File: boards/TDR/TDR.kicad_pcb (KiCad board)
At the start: 4 copper layers, 60 x 37 mm, 138 parts, among them J1 USB_C_Receptacle_USB2.0, J2 SMA, U1 LFE5UM5G-45-CABGA381, U10 W25Q128JVPIQ, U11 93LCxxBxxOT, U12 FT2232HL, U13 MIC5504-3.3YM5, U14 Resistive_Power_Divider, U15 MCP4822, U2 USBLC6-2SC6, U3 AxxDBF1-200.0000, U4 TLV3541, U5 MIC5504-3.3YM5, U6 AP3402, U7 AP3402, U8 LD39050PUR, U9 LD39050PUR, Y1 12MHz

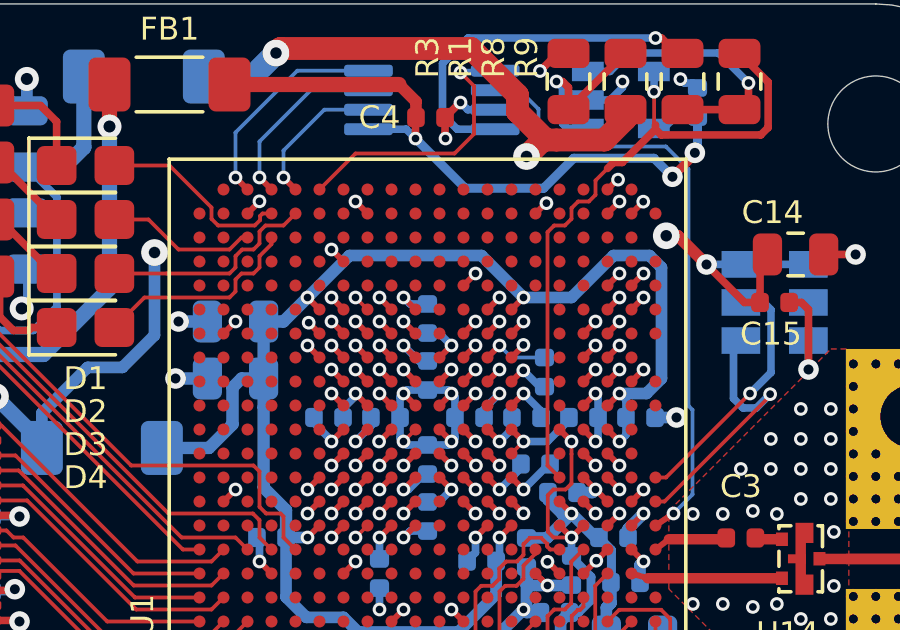
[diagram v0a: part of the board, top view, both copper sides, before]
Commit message: finishing touches on the silkscreen
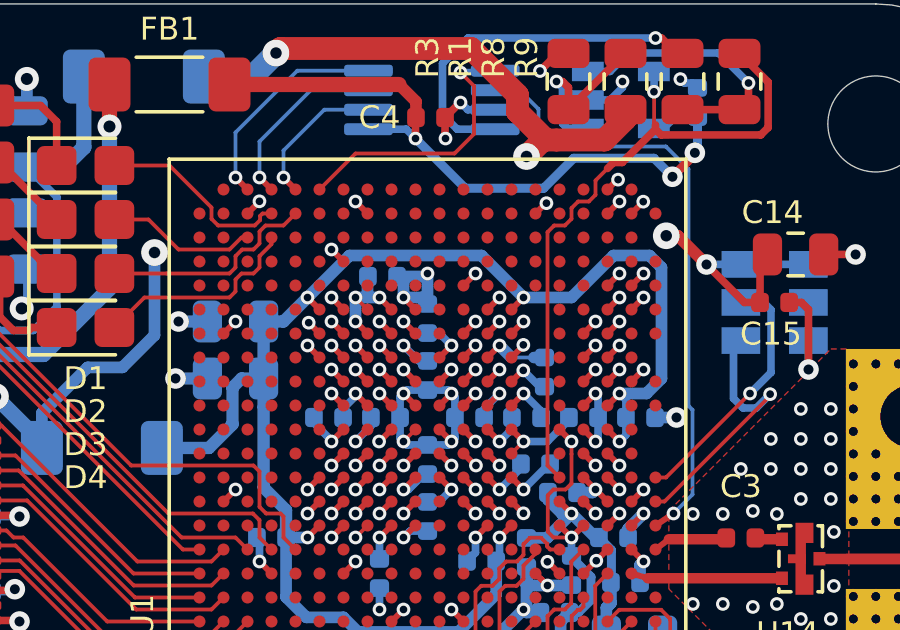
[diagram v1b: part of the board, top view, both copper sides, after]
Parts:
- added C25: 100n, Capacitor_SMD:C_0402_1005Metric, B.Cu at (146.6, 72.1)
- moved REF** 22.2 mm to (119.3, 91.0)
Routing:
- net GND: track 203.9 -> 206.8 mm, vias 183 -> 184
- net +3V3: track 54.2 -> 55.8 mm

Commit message: hopefully PCB is done
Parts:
- added C27: 1u, Capacitor_SMD:C_0805_2012Metric, B.Cu at (137.9, 85.8)
- added C29: 1u, Capacitor_SMD:C_0805_2012Metric, B.Cu at (137.9, 80.0)
- added C31: 100n, Capacitor_SMD:C_0402_1005Metric, F.Cu at (151.2, 65.9)
- added TP1: TestPoint, TestPoint:TestPoint_Pad_D1.0mm, F.Cu at (158.7, 86.6)
- added U16: MIC5504-3.3YM5, Package_TO_SOT_SMD:SOT-23-5, B.Cu at (137.9, 82.9)
- moved FB1 2.04 mm to (141.5, 66.1), turned to 180 degrees
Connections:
- C4 pad 1: Net-(C23-Pad1) -> Net-(C29-Pad1)
- C58 pad 2: Net-(C58-Pad2) -> /FT2232H/3.3V_FTDI
- FB1 pad 1: /5V_INPUT -> Net-(C29-Pad1)
- R32 pad 1: Net-(C58-Pad2) -> /FT2232H/3.3V_FTDI
- R34 pad 1: Net-(C58-Pad2) -> /FT2232H/3.3V_FTDI
- R35 pad 1: Net-(C58-Pad2) -> /FT2232H/3.3V_FTDI
- U1 pad T8: /OUT_A -> /OUT_B
- U1 pad Y6: /OUT_B -> /OUT_A
- U11 pad 6: Net-(C58-Pad2) -> /FT2232H/3.3V_FTDI
- U15 pad 1: Net-(C23-Pad1) -> Net-(C29-Pad1)
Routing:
- net Net-(C29-Pad1): track 0.00 -> 30.2 mm, vias 0 -> 2
- net /FT2232H/3.3V_FTDI: track 88.6 -> 106.3 mm, vias 5 -> 6
- net /5V_INPUT: track 118.0 -> 128.2 mm, vias 7 -> 6
- net Net-(C58-Pad2): track 7.62 -> 0.00 mm
- net Net-(TP1-Pad1): track 0.00 -> 5.28 mm
- net /OUT_B: track 20.5 -> 16.0 mm
- net GND: track 206.8 -> 211.1 mm, vias 184 -> 187
- net /OUT_A: track 22.7 -> 25.8 mm, vias 1 -> 2
- net Net-(C31-Pad2): track 6.29 -> 7.87 mm
- net Net-(C23-Pad1): track 23.3 -> 24.8 mm
- net /FT2232H/1.8V: track 37.1 -> 38.2 mm
- net +2V5: track 121.7 -> 121.0 mm
- net /VCCA: track 47.7 -> 48.2 mm
- net /~CS: track 9.34 -> 9.47 mm, vias 1 -> 3

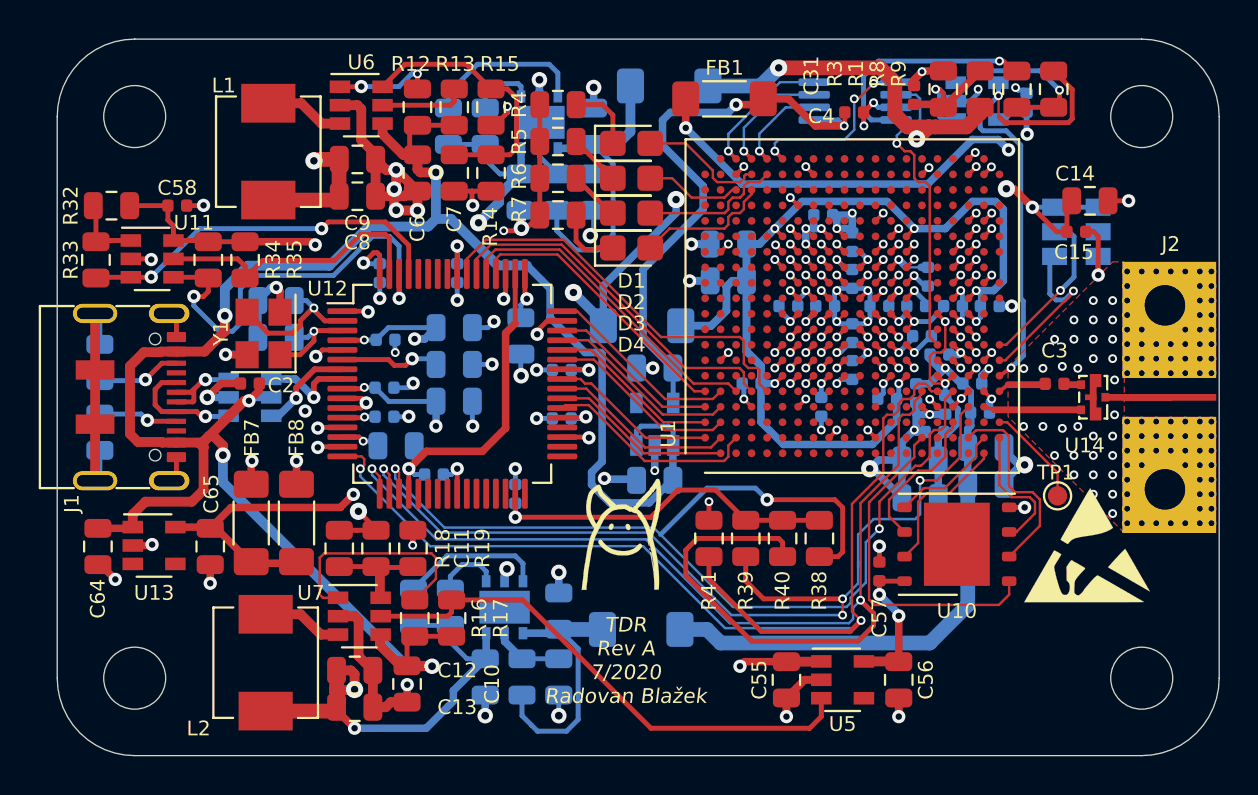
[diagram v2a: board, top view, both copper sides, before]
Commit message: Add LD39050PUR feedback resistor values, fixed regulator enable
Fixes #1
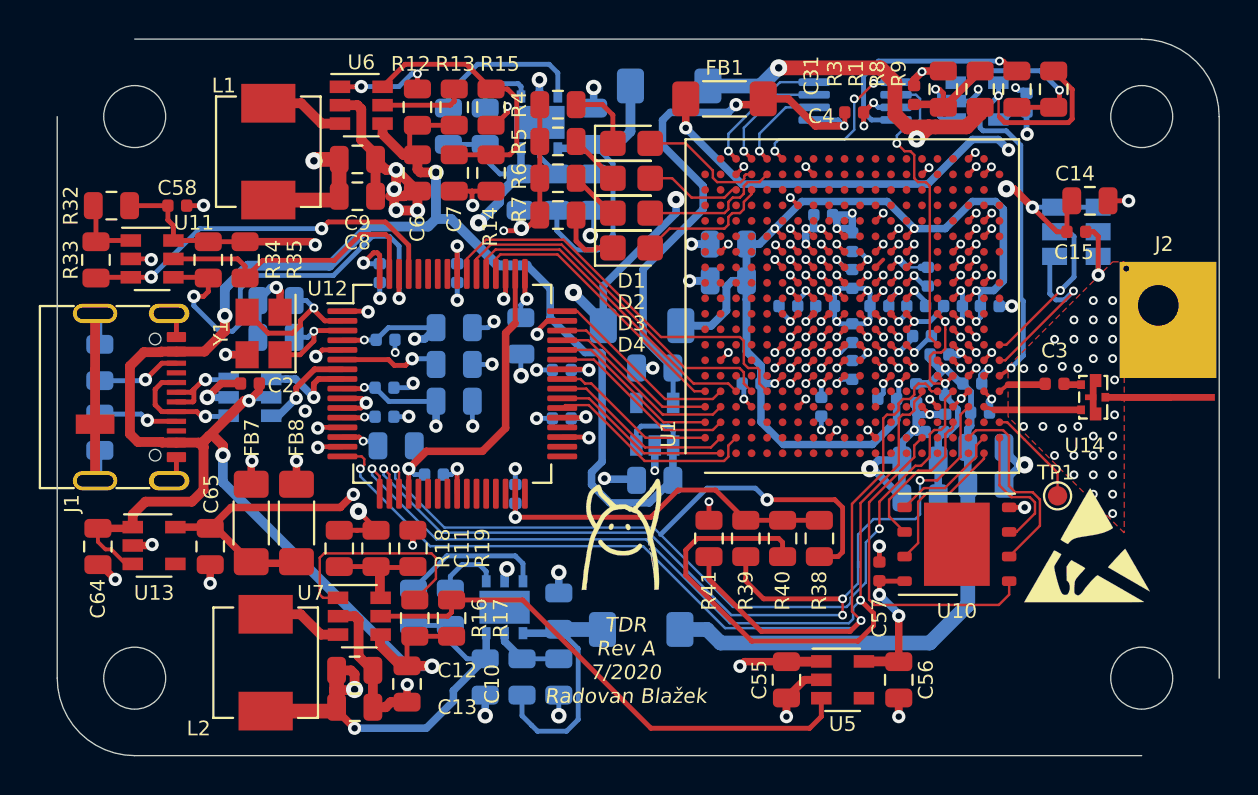
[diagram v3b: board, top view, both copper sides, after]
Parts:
- R1, R3, R8, R9: value 470 -> 4.7k
- R24, R26: value TBD -> 24k
- R25, R27: value TBD -> 47k
- U3: value AxxDBF1-200.0000 -> AK5DBF1-200.0000
- U4: value TLV3541 -> MCP6V81T-E/OT
- moved J2 0.34 mm to (164.2, 81.5)
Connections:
- net /FPGA_PROGRAMN renamed Net-(U1-PadW3)
- U1 pad A10: Net-(U1-PadA10) -> (no net)
- U1 pad A11: Net-(U1-PadA11) -> (no net)
- U1 pad A12: Net-(U1-PadA12) -> (no net)
- U1 pad A13: Net-(U1-PadA13) -> (no net)
- U1 pad A14: Net-(U1-PadA14) -> (no net)
- U1 pad A15: Net-(U1-PadA15) -> (no net)
- U1 pad A16: Net-(U1-PadA16) -> (no net)
- U1 pad A17: Net-(U1-PadA17) -> (no net)
- U1 pad A18: Net-(U1-PadA18) -> (no net)
- U1 pad A19: Net-(U1-PadA19) -> (no net)
- U1 pad A6: Net-(U1-PadA6) -> (no net)
- U1 pad A7: Net-(U1-PadA7) -> (no net)
- U1 pad A8: Net-(U1-PadA8) -> (no net)
- U1 pad A9: Net-(U1-PadA9) -> (no net)
- U1 pad B10: Net-(U1-PadB10) -> (no net)
- U1 pad B11: Net-(U1-PadB11) -> (no net)
- U1 pad B12: Net-(U1-PadB12) -> (no net)
- U1 pad B13: Net-(U1-PadB13) -> (no net)
- U1 pad B15: Net-(U1-PadB15) -> (no net)
- U1 pad B16: Net-(U1-PadB16) -> (no net)
- U1 pad B17: Net-(U1-PadB17) -> (no net)
- U1 pad B18: Net-(U1-PadB18) -> (no net)
- U1 pad B19: Net-(U1-PadB19) -> (no net)
- U1 pad B20: Net-(U1-PadB20) -> (no net)
- U1 pad B6: Net-(U1-PadB6) -> (no net)
- U1 pad B8: Net-(U1-PadB8) -> (no net)
- U1 pad B9: Net-(U1-PadB9) -> (no net)
- U1 pad C10: Net-(U1-PadC10) -> (no net)
- U1 pad C11: Net-(U1-PadC11) -> (no net)
- U1 pad C12: Net-(U1-PadC12) -> (no net)
- U1 pad C13: Net-(U1-PadC13) -> (no net)
- U1 pad C14: Net-(U1-PadC14) -> (no net)
- U1 pad C15: Net-(U1-PadC15) -> (no net)
- U1 pad C16: Net-(U1-PadC16) -> (no net)
- U1 pad C17: Net-(U1-PadC17) -> (no net)
- U1 pad C6: Net-(U1-PadC6) -> (no net)
- U1 pad C7: Net-(U1-PadC7) -> (no net)
- U1 pad C8: Net-(U1-PadC8) -> (no net)
- U1 pad C9: Net-(U1-PadC9) -> (no net)
- U1 pad D10: Net-(U1-PadD10) -> (no net)
- U1 pad D11: Net-(U1-PadD11) -> (no net)
- U1 pad D12: Net-(U1-PadD12) -> (no net)
- U1 pad D13: Net-(U1-PadD13) -> (no net)
- U1 pad D14: Net-(U1-PadD14) -> (no net)
- U1 pad D15: Net-(U1-PadD15) -> (no net)
- U1 pad D16: Net-(U1-PadD16) -> (no net)
- U1 pad D6: Net-(U1-PadD6) -> (no net)
- U1 pad D7: Net-(U1-PadD7) -> (no net)
- U1 pad D8: Net-(U1-PadD8) -> (no net)
- U1 pad D9: Net-(U1-PadD9) -> (no net)
- U1 pad E10: Net-(U1-PadE10) -> (no net)
- U1 pad E11: Net-(U1-PadE11) -> (no net)
- U1 pad E12: Net-(U1-PadE12) -> (no net)
- U1 pad E13: Net-(U1-PadE13) -> (no net)
- U1 pad E14: Net-(U1-PadE14) -> (no net)
- U1 pad E15: Net-(U1-PadE15) -> (no net)
- U1 pad E6: Net-(U1-PadE6) -> (no net)
- U1 pad E7: Net-(U1-PadE7) -> (no net)
- U1 pad E8: Net-(U1-PadE8) -> (no net)
- U1 pad E9: Net-(U1-PadE9) -> (no net)
- U1 pad F1: Net-(U1-PadF1) -> (no net)
- U1 pad F10: Net-(U1-PadF10) -> (no net)
- U1 pad F11: Net-(U1-PadF11) -> (no net)
- U1 pad F12: Net-(U1-PadF12) -> (no net)
- U1 pad F9: Net-(U1-PadF9) -> (no net)
- U1 pad G1: Net-(U1-PadG1) -> (no net)
- U1 pad G2: Net-(U1-PadG2) -> (no net)
- U1 pad H1: Net-(U1-PadH1) -> (no net)
- U1 pad H2: Net-(U1-PadH2) -> (no net)
- U1 pad J1: Net-(U1-PadJ1) -> (no net)
- U1 pad J3: Net-(U1-PadJ3) -> (no net)
- U1 pad J4: Net-(U1-PadJ4) -> (no net)
- U1 pad J5: Net-(U1-PadJ5) -> (no net)
- U1 pad K1: Net-(U1-PadK1) -> (no net)
- U1 pad K2: Net-(U1-PadK2) -> (no net)
- U1 pad K3: Net-(U1-PadK3) -> (no net)
- U1 pad K4: Net-(U1-PadK4) -> (no net)
- U1 pad K5: Net-(U1-PadK5) -> (no net)
- U1 pad L1: Net-(U1-PadL1) -> (no net)
- U1 pad L14: Net-(U1-PadL14) -> (no net)
- U1 pad L15: Net-(U1-PadL15) -> (no net)
- U1 pad L16: Net-(U1-PadL16) -> (no net)
- U1 pad L17: Net-(U1-PadL17) -> (no net)
- U1 pad L18: Net-(U1-PadL18) -> (no net)
- U1 pad L19: Net-(U1-PadL19) -> (no net)
- U1 pad L2: Net-(U1-PadL2) -> (no net)
- U1 pad L20: Net-(U1-PadL20) -> (no net)
- U1 pad L3: Net-(U1-PadL3) -> (no net)
- U1 pad L4: Net-(U1-PadL4) -> (no net)
- U1 pad L5: Net-(U1-PadL5) -> (no net)
- U1 pad L6: Net-(U1-PadL6) -> (no net)
- U1 pad L7: Net-(U1-PadL7) -> (no net)
- U1 pad M1: Net-(U1-PadM1) -> (no net)
- U1 pad M15: Net-(U1-PadM15) -> (no net)
- U1 pad M17: Net-(U1-PadM17) -> (no net)
- U1 pad M18: Net-(U1-PadM18) -> (no net)
- U1 pad M19: Net-(U1-PadM19) -> (no net)
- U1 pad M20: Net-(U1-PadM20) -> (no net)
- U1 pad M3: Net-(U1-PadM3) -> (no net)
- U1 pad M4: Net-(U1-PadM4) -> (no net)
- U1 pad M5: Net-(U1-PadM5) -> (no net)
- U1 pad M6: Net-(U1-PadM6) -> (no net)
- U1 pad N1: Net-(U1-PadN1) -> (no net)
- U1 pad N16: Net-(U1-PadN16) -> (no net)
- U1 pad N17: Net-(U1-PadN17) -> (no net)
- U1 pad N18: Net-(U1-PadN18) -> (no net)
- U1 pad N19: Net-(U1-PadN19) -> (no net)
- U1 pad N2: Net-(U1-PadN2) -> (no net)
- U1 pad N20: Net-(U1-PadN20) -> (no net)
- U1 pad N3: Net-(U1-PadN3) -> (no net)
- U1 pad N4: Net-(U1-PadN4) -> (no net)
- U1 pad N5: Net-(U1-PadN5) -> (no net)
- U1 pad P1: Net-(U1-PadP1) -> (no net)
- U1 pad P16: Net-(U1-PadP16) -> (no net)
- U1 pad P17: Net-(U1-PadP17) -> (no net)
- U1 pad P18: Net-(U1-PadP18) -> (no net)
- U1 pad P19: Net-(U1-PadP19) -> (no net)
- U1 pad P2: Net-(U1-PadP2) -> (no net)
- U1 pad P20: Net-(U1-PadP20) -> (no net)
- U1 pad P3: Net-(U1-PadP3) -> (no net)
- U1 pad P4: Net-(U1-PadP4) -> (no net)
- U1 pad P5: Net-(U1-PadP5) -> (no net)
- U1 pad R16: Net-(U1-PadR16) -> (no net)
- U1 pad R17: Net-(U1-PadR17) -> (no net)
- U1 pad R18: Net-(U1-PadR18) -> (no net)
- U1 pad R20: Net-(U1-PadR20) -> (no net)
- U1 pad T16: Net-(U1-PadT16) -> (no net)
- U1 pad T17: Net-(U1-PadT17) -> (no net)
- U1 pad T18: Net-(U1-PadT18) -> (no net)
- U1 pad T19: Net-(U1-PadT19) -> (no net)
- U1 pad T20: Net-(U1-PadT20) -> (no net)
- U1 pad U16: Net-(U1-PadU16) -> (no net)
- U1 pad U17: Net-(U1-PadU17) -> (no net)
- U1 pad U18: Net-(U1-PadU18) -> (no net)
- U1 pad U19: Net-(U1-PadU19) -> (no net)
- U1 pad U20: Net-(U1-PadU20) -> (no net)
- U1 pad W10: Net-(U1-PadW10) -> (no net)
- U1 pad W11: Net-(U1-PadW11) -> (no net)
- U1 pad W13: Net-(U1-PadW13) -> (no net)
- U1 pad W14: Net-(U1-PadW14) -> (no net)
- U1 pad W17: Net-(U1-PadW17) -> (no net)
- U1 pad W18: Net-(U1-PadW18) -> (no net)
- U1 pad W20: Net-(U1-PadW20) -> (no net)
- U1 pad Y14: Net-(U1-PadY14) -> (no net)
- U1 pad Y15: Net-(U1-PadY15) -> (no net)
- U1 pad Y16: Net-(U1-PadY16) -> (no net)
- U1 pad Y17: Net-(U1-PadY17) -> (no net)
- U1 pad Y19: Net-(U1-PadY19) -> (no net)
- U13 pad 3: /FT2232H/2.5V_PG -> /5V_INPUT
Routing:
- net /5V_INPUT: track 128.2 -> 131.1 mm
- net GND: track 211.1 -> 210.4 mm
- net +1V2_CORE: vias 22 -> 21
